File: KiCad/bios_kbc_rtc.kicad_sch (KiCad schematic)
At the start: 44 parts, among them J1 PS/2 Dual Port, U1 8242KBD, U10 BANK0, U11 BANK0, U12 BANK1, U13 BANK1, U2 74HC05, U3 SST39SF010A, U4 DS12885, Y2 32768Hz

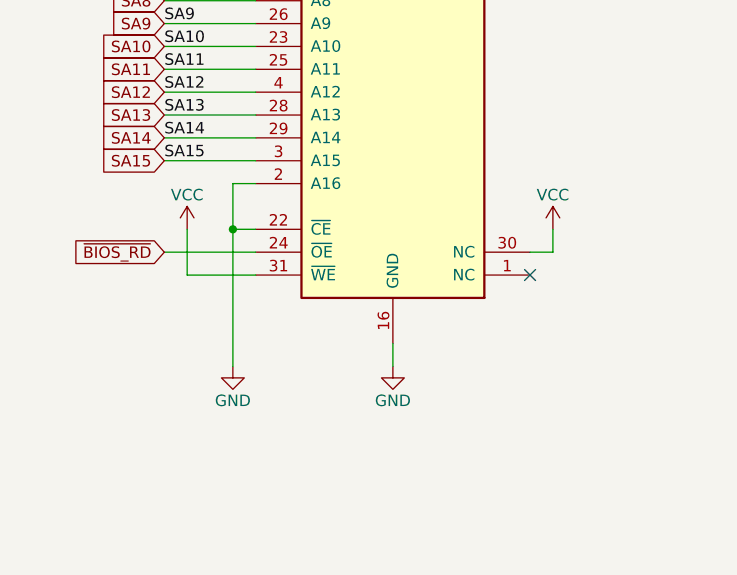
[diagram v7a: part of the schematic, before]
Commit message: Connect /OE and /WE of the BIOS ROM to allow Flash ROM in-system programming; Rotate the PCB into portrait orientation
Signed-off-by: Sergey Kiselev <sergey.kiselev@intel.com>
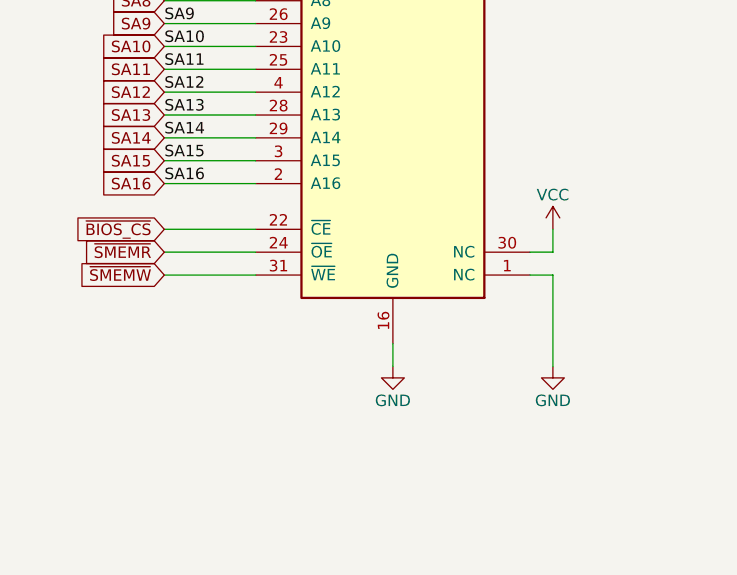
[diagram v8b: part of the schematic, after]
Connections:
- net GND: now also U3.1 (NC); no longer U3.2 (A16), U3.22 (~{CE})
- net VCC: no longer U3.31 (~{WE})
- net ~{BIOS_RD} renamed ~{SMEMR}
- new net SA16: U3.2 (A16)
- new net ~{BIOS_CS}: U3.22 (~{CE})
- new net ~{SMEMW}: U3.31 (~{WE})
- no-connect marks 13 -> 12
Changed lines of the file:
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@@
   (junction (at 177.8 48.26) (diameter 0) (color 0 0 0 0)
   )
-  (junction (at 38.1 226.06) (diameter 0) (color 0 0 0 0)
-  )
   (junction (at 330.2 93.98) (diameter 0) (color 0 0 0 0)
   )
@@
   (no_connect (at 76.2 76.2))
   (no_connect (at 152.4 208.28))
-  (no_connect (at 71.12 231.14))
   (no_connect (at 254 50.8))
   (no_connect (at 254 68.58))
@@
     (stroke (width 0) (type default) (color 0 0 0 0))
   )
-  (wire (pts (xy 38.1 220.98) (xy 38.1 226.06))
-    (stroke (width 0) (type default) (color 0 0 0 0))
-  )
   (wire (pts (xy 210.82 246.38) (xy 198.12 246.38))
     (stroke (width 0) (type default) (color 0 0 0 0))
@@
     (stroke (width 0) (type default) (color 0 0 0 0))
   )
-  (wire (pts (xy 38.1 226.06) (xy 38.1 241.3))
-    (stroke (width 0) (type default) (color 0 0 0 0))
-  )
   (wire (pts (xy 304.8 68.58) (xy 302.26 68.58))
     (stroke (width 0) (type default) (color 0 0 0 0))
@@
     (stroke (width 0) (type default) (color 0 0 0 0))
   )
-  (wire (pts (xy 40.64 220.98) (xy 38.1 220.98))
+  (wire (pts (xy 30.48 220.98) (xy 40.64 220.98))
     (stroke (width 0) (type default) (color 0 0 0 0))
   )
@@
     (stroke (width 0) (type default) (color 0 0 0 0))
   )
+  (wire (pts (xy 71.12 231.14) (xy 73.66 231.14))
+    (stroke (width 0) (type default) (color 0 0 0 0))
+  )
   (wire (pts (xy 233.68 170.18) (xy 233.68 172.72))
     (stroke (width 0) (type default) (color 0 0 0 0))
@@
     (stroke (width 0) (type default) (color 0 0 0 0))
   )
+  (wire (pts (xy 30.48 228.6) (xy 40.64 228.6))
+    (stroke (width 0) (type default) (color 0 0 0 0))
+  )
   (wire (pts (xy 208.28 220.98) (xy 220.98 220.98))
     (stroke (width 0) (type default) (color 0 0 0 0))
@@
     (stroke (width 0) (type default) (color 0 0 0 0))
   )
-  (wire (pts (xy 38.1 226.06) (xy 40.64 226.06))
-    (stroke (width 0) (type default) (color 0 0 0 0))
-  )
   (wire (pts (xy 350.52 213.36) (xy 353.06 213.36))
     (stroke (width 0) (type default) (color 0 0 0 0))
@@
     (stroke (width 0) (type default) (color 0 0 0 0))
   )
-  (wire (pts (xy 30.48 228.6) (xy 40.64 228.6))
+  (wire (pts (xy 30.48 226.06) (xy 40.64 226.06))
     (stroke (width 0) (type default) (color 0 0 0 0))
   )
@@
     (stroke (width 0) (type default) (color 0 0 0 0))
   )
+  (wire (pts (xy 73.66 231.14) (xy 73.66 241.3))
+    (stroke (width 0) (type default) (color 0 0 0 0))
+  )
   (wire (pts (xy 208.28 218.44) (xy 220.98 218.44))
     (stroke (width 0) (type default) (color 0 0 0 0))
@@
     (stroke (width 0) (type default) (color 0 0 0 0))
   )
-  (wire (pts (xy 33.02 226.06) (xy 33.02 231.14))
-    (stroke (width 0) (type default) (color 0 0 0 0))
-  )
   (wire (pts (xy 226.06 254) (xy 231.14 254))
     (stroke (width 0) (type default) (color 0 0 0 0))
@@
     (stroke (width 0) (type default) (color 0 0 0 0))
   )
-  (wire (pts (xy 40.64 231.14) (xy 33.02 231.14))
+  (wire (pts (xy 40.64 231.14) (xy 30.48 231.14))
     (stroke (width 0) (type default) (color 0 0 0 0))
   )
@@
     (effects (font (size 1.27 1.27)) (justify right bottom))
   )
+  (label "SA16" (at 30.48 220.98 0)
+    (effects (font (size 1.27 1.27)) (justify left bottom))
+  )
   (label "RA0" (at 208.28 180.34 0)
     (effects (font (size 1.27 1.27)) (justify left bottom))
@@
     )
   )
+  (global_label "~{SMEMR}" (shape input) (at 30.48 228.6 180) (fields_autoplaced)
+    (effects (font (size 1.27 1.27)) (justify right))
+    (property "Intersheet References" "${INTERSHEET_REFS}" (id 0) (at 21.5355 228.5206 0)
+      (effects (font (size 1.27 1.27)) (justify right) hide)
+    )
+  )
   (global_label "SA15" (shape input) (at 30.48 218.44 180) (fields_autoplaced)
     (effects (font (size 1.27 1.27)) (justify right))
@@
     )
   )
-  (global_label "~{BIOS_RD}" (shape input) (at 30.48 228.6 180) (fields_autoplaced)
+  (global_label "~{BIOS_CS}" (shape input) (at 30.48 226.06 180) (fields_autoplaced)
     (effects (font (size 1.27 1.27)) (justify right))
-    (property "Intersheet References" "${INTERSHEET_REFS}" (id 0) (at 20.1445 228.5206 0)
+    (property "Intersheet References" "${INTERSHEET_REFS}" (id 0) (at 20.205 225.9806 0)
       (effects (font (size 1.27 1.27)) (justify right) hide)
     )
@@
     )
   )
+  (global_label "SA16" (shape input) (at 30.48 220.98 180) (fields_autoplaced)
+    (effects (font (size 1.27 1.27)) (justify right))
+    (property "Intersheet References" "${INTERSHEET_REFS}" (id 0) (at 23.3498 220.9006 0)
+      (effects (font (size 1.27 1.27)) (justify right) hide)
+    )
+  )
   (global_label "~{IOW}" (shape input) (at 208.28 101.6 180) (fields_autoplaced)
     (effects (font (size 1.27 1.27)) (justify right))
@@
     )
   )
+  (global_label "~{SMEMW}" (shape input) (at 30.48 231.14 180) (fields_autoplaced)
+    (effects (font (size 1.27 1.27)) (justify right))
+    (property "Intersheet References" "${INTERSHEET_REFS}" (id 0) (at 21.354 231.0606 0)
+      (effects (font (size 1.27 1.27)) (justify right) hide)
+    )
+  )
   (global_label "~{MCAS2}" (shape input) (at 226.06 261.62 180) (fields_autoplaced)
     (effects (font (size 1.27 1.27)) (justify right))
@@
     (pin "2")
   )
-  (symbol (lib_id "power:GND") (at 38.1 241.3 0) (unit 1)
-    (in_bom yes) (on_board yes)
-    (property "Reference" "#PWR0170" (id 0) (at 38.1 247.65 0)
-      (effects (font (size 1.27 1.27)) hide)
-    )
-    (property "Value" "GND" (id 1) (at 38.1 245.11 0))
-    (property "Footprint" "" (id 2) (at 38.1 241.3 0)
-      (effects (font (size 1.27 1.27)) hide)
-    )
-    (property "Datasheet" "" (id 3) (at 38.1 241.3 0)
-      (effects (font (size 1.27 1.27)) hide)
-    )
-    (pin "1")
-  )
   (symbol (lib_id "Device:R") (at 275.59 254 90) (unit 1)
     (in_bom yes) (on_board yes)
@@
     (pin "1")
   )
+  (symbol (lib_id "power:GND") (at 73.66 241.3 0) (unit 1)
+    (in_bom yes) (on_board yes)
+    (property "Reference" "#PWR?" (id 0) (at 73.66 247.65 0)
+      (effects (font (size 1.27 1.27)) hide)
+    )
+    (property "Value" "GND" (id 1) (at 73.66 245.11 0))
+    (property "Footprint" "" (id 2) (at 73.66 241.3 0)
+      (effects (font (size 1.27 1.27)) hide)
+    )
+    (property "Datasheet" "" (id 3) (at 73.66 241.3 0)
+      (effects (font (size 1.27 1.27)) hide)
+    )
+    (pin "1")
+  )
   (symbol (lib_id "power:VCC") (at 238.76 170.18 0) (unit 1)
     (in_bom yes) (on_board yes)
@@
     (pin "5")
   )
-  (symbol (lib_id "power:VCC") (at 33.02 226.06 0) (unit 1)
-    (in_bom yes) (on_board yes)
-    (property "Reference" "#PWR0182" (id 0) (at 33.02 229.87 0)
-      (effects (font (size 1.27 1.27)) hide)
-    )
-    (property "Value" "VCC" (id 1) (at 33.02 222.25 0))
-    (property "Footprint" "" (id 2) (at 33.02 226.06 0)
-      (effects (font (size 1.27 1.27)) hide)
-    )
-    (property "Datasheet" "" (id 3) (at 33.02 226.06 0)
-      (effects (font (size 1.27 1.27)) hide)
-    )
-    (pin "1")
-  )
   (symbol (lib_id "power:GND") (at 236.22 114.3 0) (unit 1)
